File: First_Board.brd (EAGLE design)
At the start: 69.8 x 69.8 mm, 32 parts, among them U0 F22X4---DA38, U1 TLC59108PW, U3 A1101, U4 TPS62111RSA

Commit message: Updated to add IR
git-svn-id: file:///p/svn/Projects/Boards/Driveway_Lights@58 1e7840b9-f7c2-db11-b69c-00d0b71b9132
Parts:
- added LED10, LED11, LED12, LED9: (no value), led:LED5MM
- added R13, R14: 10k, rcl:R0603
- added T1, T2: (no value), zetex:SOT-23
- added U$1, U$2: TSOP39338, opto-vishay:TSOP39338
- moved J1 6.97 mm to (14.4, 30.2)
- moved J2 6.93 mm to (17.0, 30.2), turned to 180 degrees
- moved J12 3.60 mm to (4.60, 35.0), turned to 90 degrees
- moved C1 1.96 mm to (11.8, 24.7)
- moved R1 1.14 mm to (3.58, 42.7), turned to 270 degrees
- moved C3 0.64 mm to (16.7, 15.2)
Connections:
- net N$4 renamed PG
- new net IRLED1: T1.3, U0.21
- new net IRLED2: T2.3, U0.22
- new net IR_IN1: U$1.OUT, U0.33
- new net IR_IN2: U$2.OUT, U0.34
- new net N$2: LED12.K, R14.2
- new net N$3: LED11.K, LED12.A
- new net N$4: LED10.A, LED9.K
- new net N$5: LED10.K, R13.2
- new net N$6: R13.1, T1.1
- new net N$9: R14.1, T2.1
- net 3.3V: now also LED11.A, LED9.A, U$1.VS, U$2.VS
- net GND: now also T1.2, T2.2, U$1.GND, U$2.GND
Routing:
- net VWHITE_SCALED: track 51.5 -> 85.2 mm
- net VGREEN_SCALED: track 37.1 -> 53.9 mm
- net VIN: track 89.3 -> 72.8 mm
- net 3.3V: track 115.9 -> 128.2 mm, vias 3 -> 2
- net GND: track 180.2 -> 191.5 mm
- net VBLUE_SCALED: track 50.4 -> 41.5 mm
- net LED_SCL: track 36.1 -> 29.2 mm
- net PG: track 16.1 -> 9.59 mm
- net SBWTCK: track 11.2 -> 14.1 mm
- net RF_CLK: track 29.9 -> 27.1 mm
- net BLUE: track 18.5 -> 20.0 mm
- net RESET/SBWTDIO: track 30.4 -> 31.8 mm, vias 0 -> 1
- net RF_SOMI: track 30.2 -> 31.2 mm
- net VRED_SCALED: track 43.7 -> 42.6 mm
- net N$33: track 21.9 -> 22.8 mm
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
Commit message: Adding bypass caps
git-svn-id: file:///p/svn/Projects/Boards/Driveway_Lights@59 1e7840b9-f7c2-db11-b69c-00d0b71b9132
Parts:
- removed LED10, LED11, LED12, LED9: (no value), led:LED5MM
- added C5, C6, C7: (no value), rcl:C0603
- added IR1A, IR1B, IR2A, IR2B: (no value), led:LED5MM
- R13, R14: value 10k -> 10
- moved C1 52.8 mm to (55.3, 54.6)
- moved U4 52.8 mm to (57.9, 49.5)
- moved C3 52.8 mm to (60.2, 45.1)
- moved U$1 25.1 mm to (10.1, 14.9), turned to 315 degrees
- moved U$2 17.5 mm to (59.2, 13.9), turned to 45 degrees
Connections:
- new net N$11: C6.1, U3.7
- net 3.3V: now also C5.1, C7.1, IR1B.A, IR2B.A; no longer LED11.A, LED9.A
- net GND: now also C5.2, C6.2, C7.2
- net N$2: now also IR2A.K; no longer LED12.K
- net N$3: now also IR2A.A, IR2B.K; no longer LED11.K, LED12.A
- net N$4: now also IR1A.A, IR1B.K; no longer LED10.A, LED9.K
- net N$5: now also IR1A.K; no longer LED10.K
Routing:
- net N$11: track 0.00 -> 114.3 mm, vias 0 -> 6
- net 3.3V: track 128.2 -> 241.5 mm, vias 2 -> 7
- net IR_IN2: track 0.00 -> 88.4 mm, vias 0 -> 1
- net IRLED2: track 0.00 -> 80.0 mm, vias 0 -> 4
- net IRLED1: track 0.00 -> 50.8 mm, vias 0 -> 2
- net PG: track 9.59 -> 57.2 mm
- net GND: track 191.5 -> 237.8 mm, vias 1 -> 2
- net IR_IN1: track 0.00 -> 37.0 mm, vias 0 -> 2
- net N$4: track 0.00 -> 31.6 mm
- net N$6: track 0.00 -> 29.0 mm
- net N$3: track 0.00 -> 24.9 mm
- net N$5: track 0.00 -> 22.5 mm, vias 0 -> 1
- net VIN: track 72.8 -> 53.5 mm
- net N$31: track 34.5 -> 20.9 mm, vias 0 -> 2
- net N$2: track 0.00 -> 12.7 mm
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
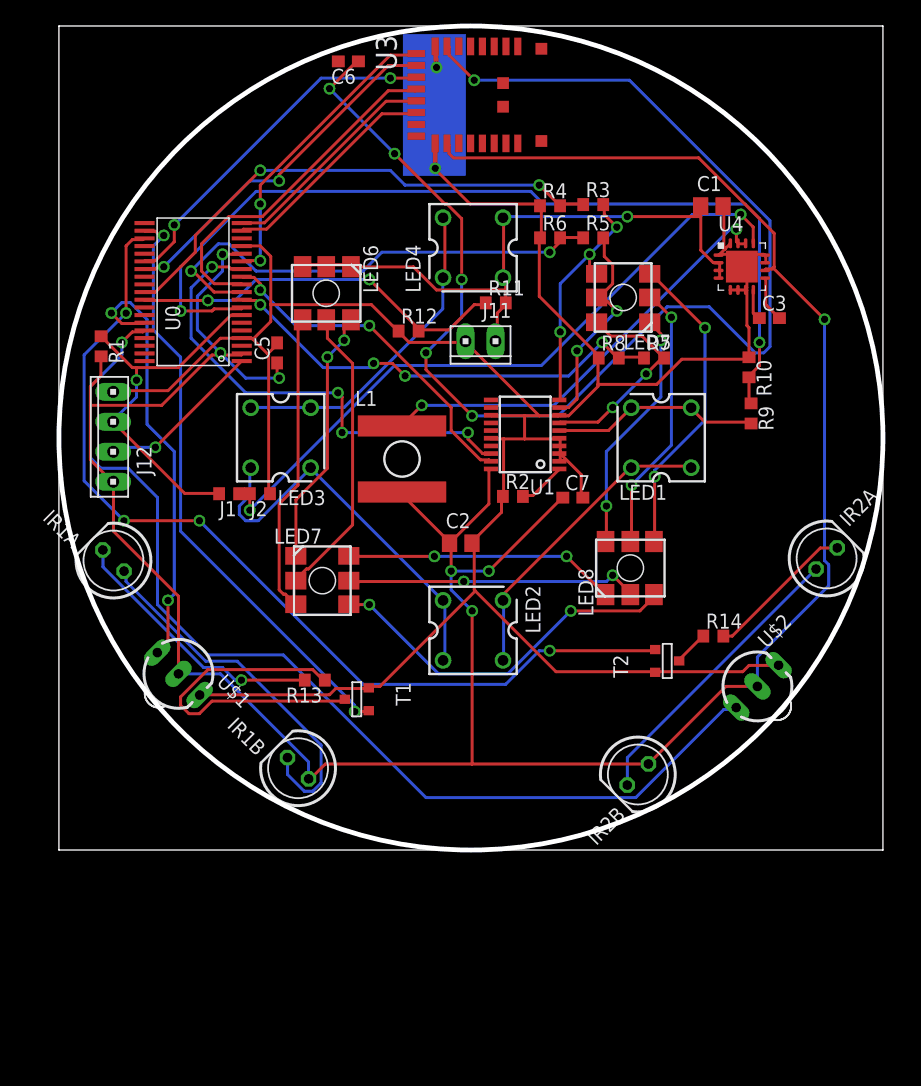
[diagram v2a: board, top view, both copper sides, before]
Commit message: Adding IR LED/Detector (and maybe the bottom RGB leds if not already committed
git-svn-id: file:///p/svn/Projects/Boards/Driveway_Lights@60 1e7840b9-f7c2-db11-b69c-00d0b71b9132
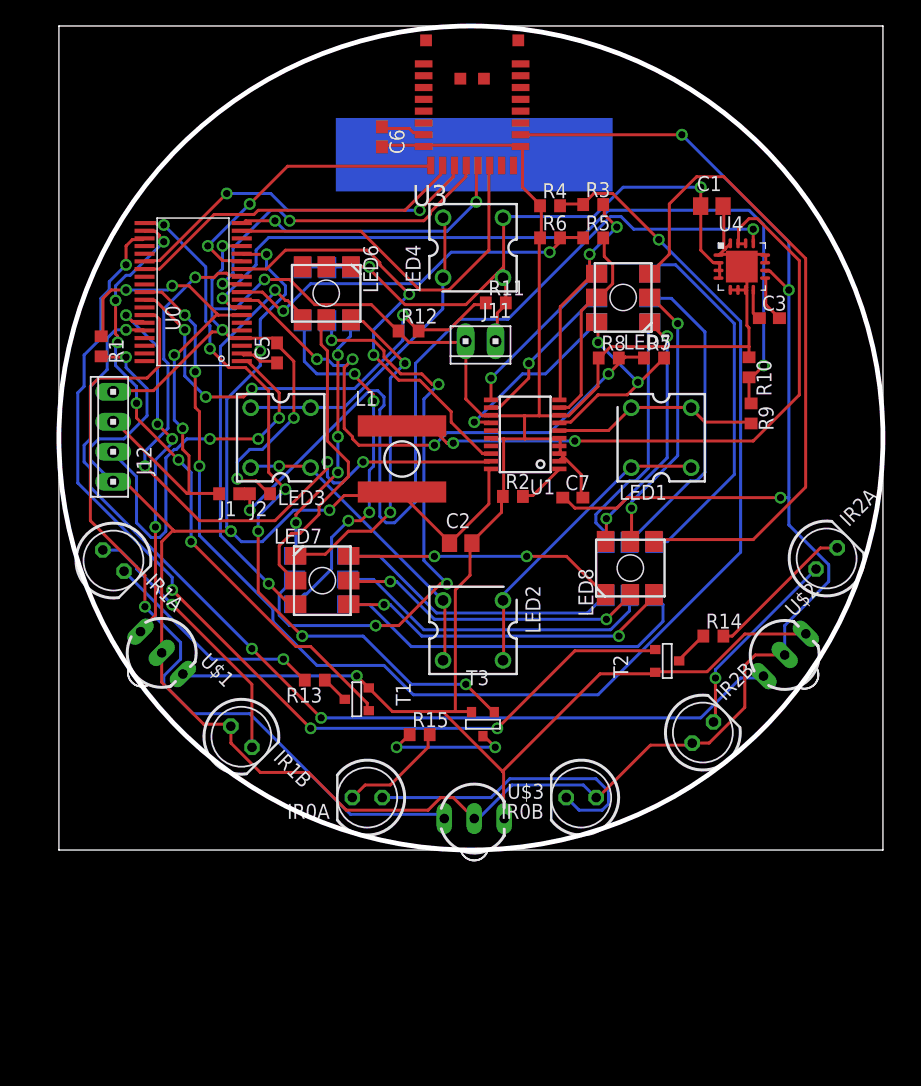
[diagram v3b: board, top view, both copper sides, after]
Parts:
- added IR0A, IR0B: (no value), led:LED5MM
- added LED10, LED11, LED12, LED9: CLP6C, led:CLP6C
- added R15: 10, rcl:R0603
- added T3: (no value), zetex:SOT-23
- added U$3: TSOP39338, opto-vishay:TSOP39338
- moved C6 7.00 mm to (27.4, 60.5), turned to 270 degrees
- moved IR2B 6.56 mm to (54.6, 9.96), turned to 45 degrees
- moved IR1B 5.49 mm to (15.5, 9.60), turned to 315 degrees
- moved U$2 3.53 mm to (61.5, 16.5)
- moved U$1 2.28 mm to (8.71, 16.7)
- moved U3 1.27 mm to (35.0, 64.0), turned to 0 degrees
- turned IR1A to 315 degrees
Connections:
- new net BLUE2: LED9.4, U1.14
- new net GREEN2: LED9.5, U1.12
- new net IRLED0: T3.3, U0.20
- new net IR_IN0: U$3.OUT, U0.32
- new net N$12: LED12.4, LED9.3
- new net N$13: LED11.4, LED12.3
- new net N$14: LED10.4, LED11.3
- new net N$15: LED10.5, LED11.2
- new net N$16: LED11.5, LED12.2
- new net N$17: LED12.5, LED9.2
- new net N$18: LED12.6, LED9.1
- new net N$20: LED11.6, LED12.1
- new net N$21: LED10.6, LED11.1
- new net N$22: IR0A.K, R15.2
- new net N$23: IR0A.A, IR0B.K
- new net N$24: R15.1, T3.1
- new net RED2: LED9.6, U1.11
- net 3.3V: now also IR0B.A, U$3.VS
- net GND: now also T3.2, U$3.GND
- net VIN: now also LED10.1, LED10.2, LED10.3
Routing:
- net N$11: track 114.3 -> 3.90 mm, vias 6 -> 0
- net VBLUE_SCALED: track 43.7 -> 120.4 mm, vias 2 -> 4
- net IR_IN0: track 0.00 -> 69.4 mm, vias 0 -> 1
- net IRLED0: track 0.00 -> 63.1 mm, vias 0 -> 6
- net N$15: track 0.00 -> 50.6 mm, vias 0 -> 4
- net N$21: track 0.00 -> 31.9 mm, vias 0 -> 4
- net N$20: track 0.00 -> 31.6 mm
- net N$18: track 0.00 -> 31.5 mm
- net N$25: track 26.5 -> 56.2 mm, vias 2 -> 0
- net GND: track 237.8 -> 267.4 mm, vias 2 -> 6
- net LED_SDA: track 29.0 -> 58.2 mm, vias 2 -> 4
- net N$16: track 0.00 -> 27.6 mm
- net N$6: track 29.0 -> 2.36 mm
- net N$17: track 0.00 -> 26.7 mm
- net N$23: track 0.00 -> 25.6 mm
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
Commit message: Adding rectifier bridge to schematic
git-svn-id: file:///p/svn/Projects/Boards/Driveway_Lights@66 1e7840b9-f7c2-db11-b69c-00d0b71b9132
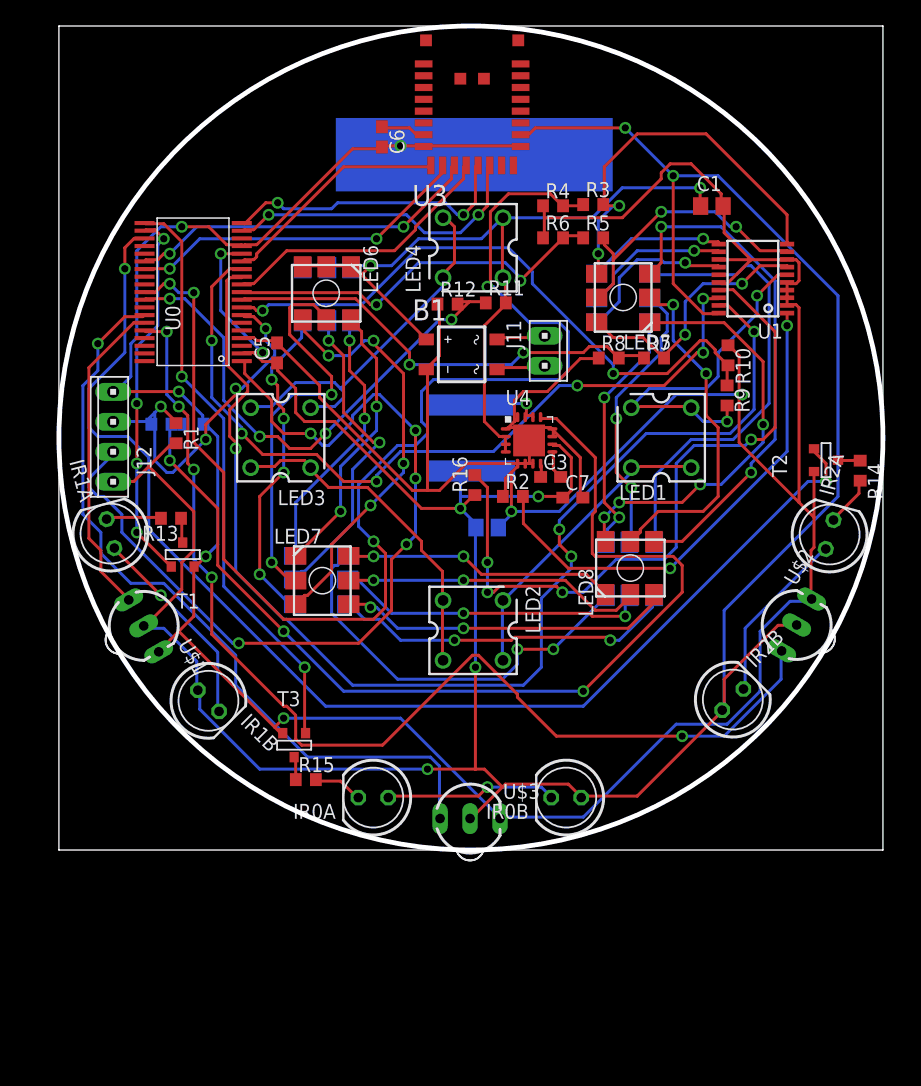
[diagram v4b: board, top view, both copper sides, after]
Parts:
- added B1: B6S, rectifier:MBS
- added R16: 10k, rcl:R0603
- moved U1 23.4 mm to (58.8, 48.4)
- moved U4 23.3 mm to (39.9, 34.7)
- moved C3 22.9 mm to (41.7, 31.6)
- moved T2 21.7 mm to (65.0, 33.0)
- moved T1 19.2 mm to (10.5, 25.0), turned to 180 degrees
- moved R14 18.7 mm to (67.9, 32.2), turned to 270 degrees
- moved R13 18.4 mm to (9.50, 28.1)
- moved T3 16.1 mm to (19.9, 8.89)
- moved R15 10.4 mm to (20.9, 5.97)
- moved R1 9.73 mm to (9.93, 35.3)
- moved J1 8.23 mm to (8.69, 36.1), flipped to the bottom, turned to 0 degrees
- moved J2 8.16 mm to (11.4, 36.1), flipped to the bottom, turned to 0 degrees
- moved L1 6.11 mm to (34.9, 34.9), flipped to the bottom
- moved J11 5.50 mm to (41.2, 42.3), turned to 270 degrees
- moved IR1B 4.13 mm to (12.7, 12.6)
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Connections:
- new net N$38: R16.2, U1.17
- new net N$39: B1.AC1, J11.2
- new net N$40: B1.AC2, J11.1
- net 3.3V: now also R16.1
- net GND: now also B1.-; no longer J11.1
- net VIN: now also B1.+; no longer J11.2
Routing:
- net GND: track 267.4 -> 350.4 mm, vias 6 -> 7
- net N$38: track 0.00 -> 59.5 mm, vias 0 -> 4
- net N$1: track 56.2 -> 6.58 mm, vias 2 -> 1
- net LED_SDA: track 58.2 -> 103.1 mm
- net SBWTCK: track 33.7 -> 75.8 mm, vias 3 -> 5
- net N$19: track 4.05 -> 42.1 mm, vias 0 -> 2
- net LED_SCL: track 36.8 -> 68.3 mm, vias 2 -> 6
- net N$15: track 50.6 -> 27.2 mm, vias 4 -> 2
- net IRLED1: track 53.6 -> 31.9 mm, vias 6 -> 4
- net IRLED2: track 84.6 -> 105.4 mm, vias 4 -> 2
- net VWHITE_SCALED: track 68.2 -> 52.9 mm
- net N$31: track 21.5 -> 36.1 mm, vias 2 -> 4
- net N$5: track 19.1 -> 4.80 mm, vias 1 -> 0
- net BLUE: track 19.7 -> 33.5 mm
- net IRLED0: track 63.1 -> 49.8 mm, vias 6 -> 2
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
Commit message: Schematic review with V
git-svn-id: file:///p/svn/Projects/Boards/Driveway_Lights@67 1e7840b9-f7c2-db11-b69c-00d0b71b9132
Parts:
- removed R16: 10k, rcl:R0603
- added C10, C4, C8, C9: (no value), rcl:C0603
- added C11: 22uF, rcl:C1210
- added L2: (no value), rcl:R0603
- C1: value 10uF -> 1uF
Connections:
- net N$11 renamed VDCOUP1
- new net N$42: L2.2, U3.18
- new net VDCOUP2: C4.1, U3.15
- net 3.3V: now also C10.1, C8.1, C9.1, L2.1; no longer R16.1, U3.18
- net GND: now also C10.2, C11.2, C4.2, C8.2, C9.2
- net N$38: no longer R16.2
- net N$7: now also U0.38; no longer C3.1, U4.8
- net VIN: now also C11.1, C3.1, U4.8
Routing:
- net GND: track 350.4 -> 0.00 mm, vias 7 -> 0
- net 3.3V: track 265.8 -> 0.00 mm, vias 8 -> 0
- net VBLUE_SCALED: track 107.8 -> 0.00 mm, vias 4 -> 0
- net IRLED2: track 105.4 -> 0.00 mm, vias 2 -> 0
- net LED_SDA: track 103.1 -> 0.00 mm, vias 4 -> 0
- net IR_IN2: track 93.1 -> 0.00 mm, vias 5 -> 0
- net PG: track 86.9 -> 0.00 mm, vias 3 -> 0
- net SBWTCK: track 75.8 -> 0.00 mm, vias 5 -> 0
- net VIN: track 74.7 -> 0.00 mm, vias 2 -> 0
- net LED_SCL: track 68.3 -> 0.00 mm, vias 6 -> 0
- net IR_IN0: track 66.0 -> 0.00 mm, vias 1 -> 0
- net N$38: track 59.5 -> 0.00 mm, vias 4 -> 0
- net VWHITE_SCALED: track 52.9 -> 0.00 mm, vias 2 -> 0
- net IRLED0: track 49.8 -> 0.00 mm, vias 2 -> 0
- net N$25: track 43.7 -> 0.00 mm, vias 2 -> 0
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
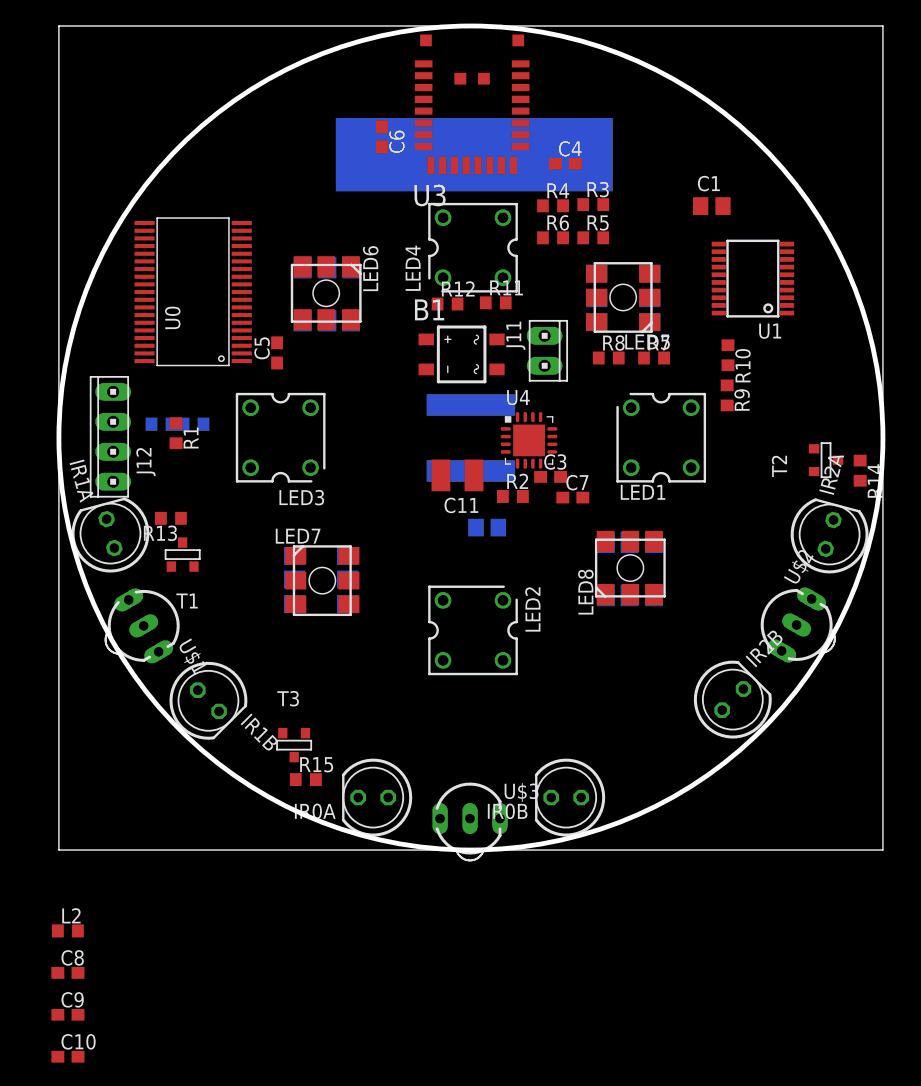
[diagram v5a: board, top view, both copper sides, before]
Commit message: Placed changes from schematic update, some manual routing, but mostly autorouted board
git-svn-id: file:///p/svn/Projects/Boards/Driveway_Lights@68 1e7840b9-f7c2-db11-b69c-00d0b71b9132
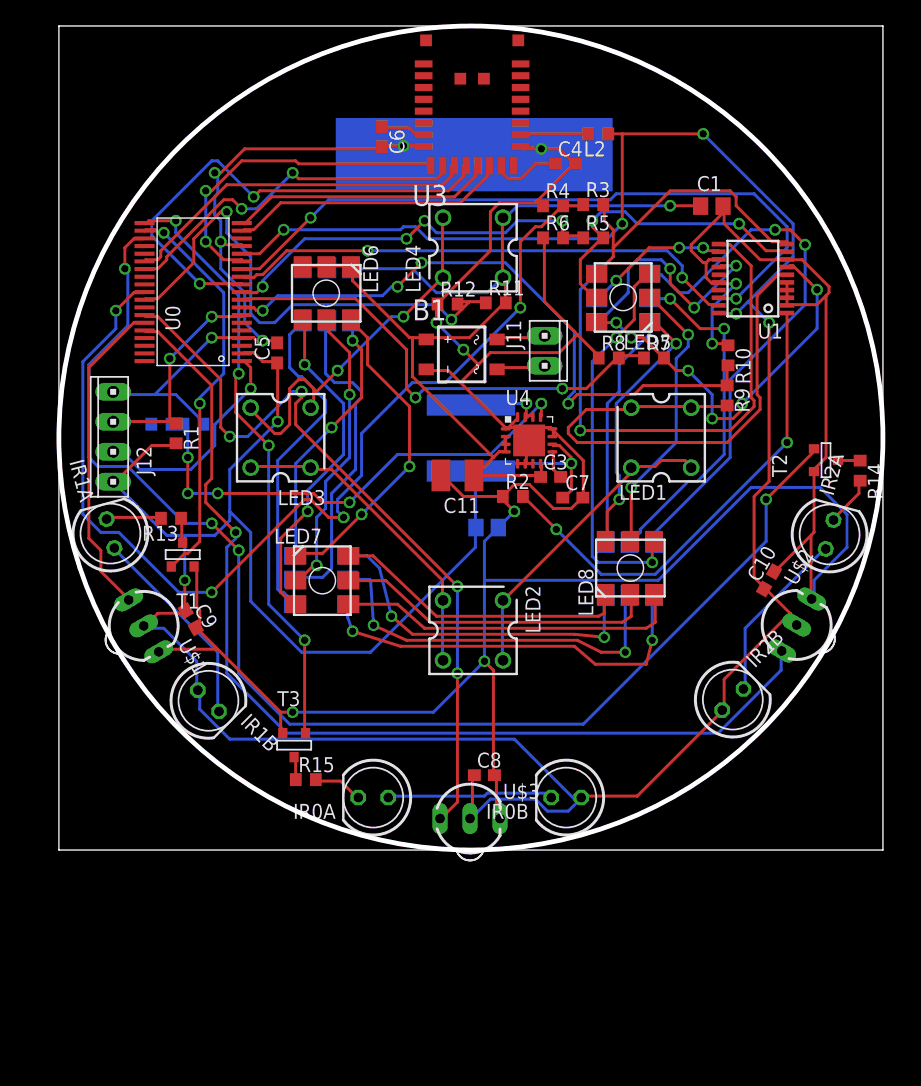
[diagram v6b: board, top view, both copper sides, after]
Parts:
- moved L2 81.2 mm to (45.7, 60.7), turned to 180 degrees
- moved C10 71.9 mm to (60.2, 22.9), turned to 60 degrees
- moved C8 39.1 mm to (36.1, 6.35)
- moved C9 35.1 mm to (11.2, 19.6), turned to 300 degrees
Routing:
- net GND: track 0.00 -> 353.3 mm, vias 0 -> 13
- net 3.3V: track 0.00 -> 291.7 mm, vias 0 -> 8
- net IRLED2: track 0.00 -> 110.1 mm, vias 0 -> 4
- net VIN: track 0.00 -> 89.8 mm, vias 0 -> 1
- net VBLUE_SCALED: track 0.00 -> 88.5 mm, vias 0 -> 4
- net IR_IN2: track 0.00 -> 86.5 mm, vias 0 -> 1
- net IR_IN0: track 0.00 -> 64.3 mm, vias 0 -> 4
- net LED_SCL: track 0.00 -> 59.4 mm, vias 0 -> 2
- net VWHITE_SCALED: track 0.00 -> 54.5 mm, vias 0 -> 4
- net IRLED0: track 0.00 -> 51.0 mm, vias 0 -> 4
- net N$18: track 0.00 -> 47.1 mm, vias 0 -> 2
- net N$10: track 0.00 -> 45.8 mm
- net RED2: track 0.00 -> 45.0 mm, vias 0 -> 1
- net LED_SDA: track 0.00 -> 43.9 mm, vias 0 -> 2
- net VIN_SCALED: track 0.00 -> 43.9 mm, vias 0 -> 2
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
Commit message: Updates?
git-svn-id: file:///p/svn/Projects/Boards/Driveway_Lights@69 1e7840b9-f7c2-db11-b69c-00d0b71b9132
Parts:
- moved R14 1.44 mm to (66.9, 31.1)
- moved C2 1.14 mm to (35.8, 26.3)
- moved R2 0.76 mm to (38.5, 29.2)
- moved C7 0.57 mm to (43.8, 29.4)
- moved C3 0.51 mm to (41.7, 31.1)
- moved T2 0.51 mm to (65.0, 33.5)
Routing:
- net GND: track 353.3 -> 357.5 mm
- net 3.3V: track 291.7 -> 293.2 mm
- net N$2: track 4.27 -> 2.83 mm
- net VIN: track 89.8 -> 90.3 mm
- net N$8: track 2.50 -> 3.01 mm
